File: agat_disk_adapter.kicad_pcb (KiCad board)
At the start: 2 copper layers, 58.4 x 50.8 mm, 9 parts, among them J1 Controller, J2_A1 IZOT FDD, J2_B2 IZOT FDD, J3 Apple II FDD, J4 Gotek, J5 Gotek power, J6 DS switch, J7 Jumper parking, J8 Controller DS2

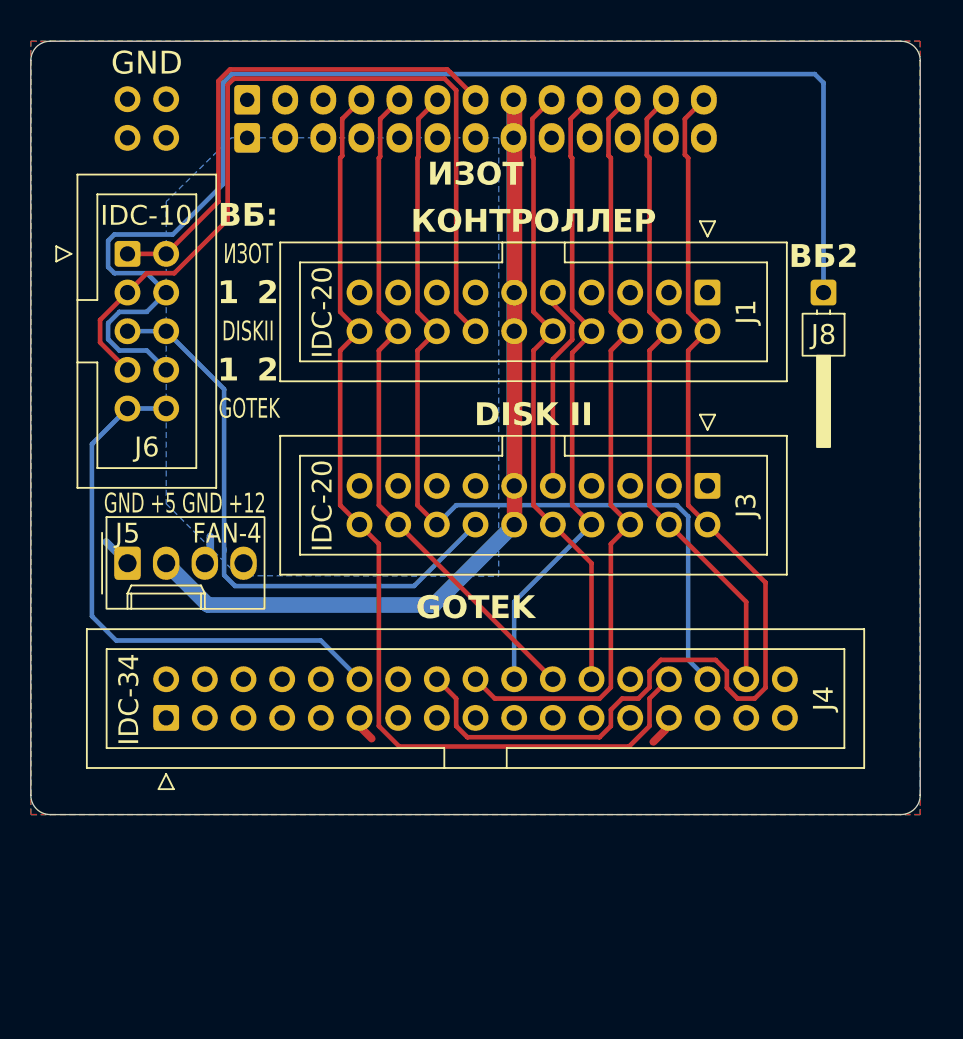
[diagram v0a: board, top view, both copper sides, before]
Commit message: one fdc connector
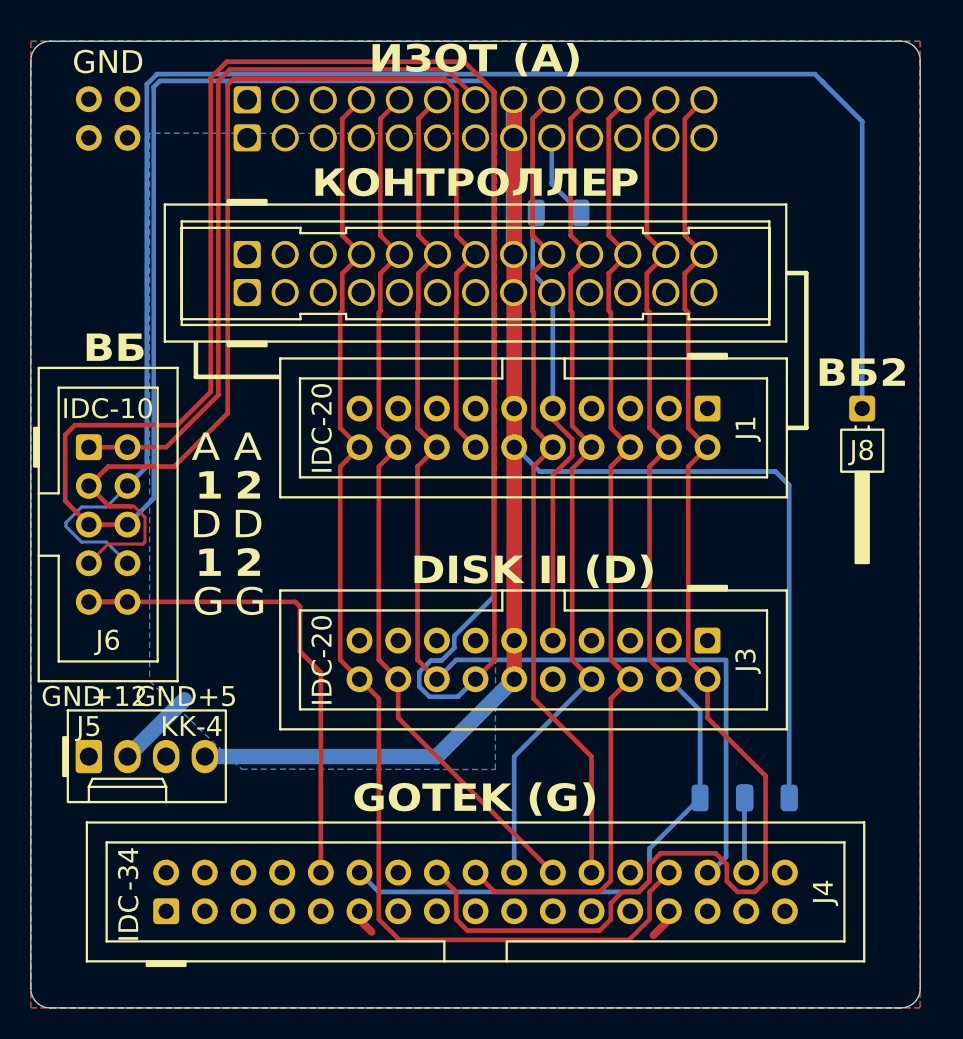
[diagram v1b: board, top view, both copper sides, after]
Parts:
- added J9_A1: КОНТРОЛЛЕР, Connector_JST:JST_EH_B13B-EH-A_1x13_P2.50mm_Vertical, F.Cu at (68.6, 55.9)
- added J9_B2: КОНТРОЛЛЕР, Connector_JST:JST_EH_B13B-EH-A_1x13_P2.50mm_Vertical, F.Cu at (68.6, 53.4)
- added R1: 0, Resistor_SMD:R_1206_3216Metric, B.Cu at (74.0, 50.6)
- added R2: 0, Resistor_SMD:R_1206_3216Metric, B.Cu at (87.7, 89.1)
- added R3: 0, Resistor_SMD:R_1206_3216Metric, B.Cu at (84.8, 89.1)
- J1: value Controller -> КОНТРОЛЛЕР
- J2_A1, J2_B2: value IZOT FDD -> ИЗОТ
- J3: value Apple II FDD -> DISK II
- J4: value Gotek -> GOTEK
- J5: value Gotek power -> Питание GOTEK
- J6: value DS switch -> ВБ
- J7: value Jumper parking -> Джамперы
- J8: value Controller DS2 -> ВБ2
- moved J5 13.0 mm to (43.2, 86.4)
- moved J6 13.0 mm to (43.2, 66.0)
- moved J4 12.7 mm to (48.3, 96.5)
- moved J3 10.2 mm to (83.8, 78.7)
- moved J8 8.03 mm to (94.0, 63.5)
- moved J1 7.62 mm to (83.8, 63.5)
- moved J7 2.54 mm to (43.2, 43.2)
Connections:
- net /DS1 renamed /EN1
- net /DS_J2 renamed /EN_J2
- net /DS_J3 renamed /EN_J3
- net /F0 renamed /PH0
- net /F2 renamed /PH2
- net /F3 renamed /PH3
- J1 pad 4: /F1 -> /PH1
- J2_A1 pad 9: unconnected-(J2_A1-Pin_9-Pad9) -> Net-(J2_A1-Pin_9)
- J2_B2 pad 12: /F1 -> /PH1
- J3 pad 4: /F1 -> /PH1
- J4 pad 10: unconnected-(J4-Pin_10-Pad10) -> /EN_J4
- J4 pad 12: /DS_J4 -> /PH1
- J4 pad 32: /F1 -> Net-(J4-Pin_32)
- J5 pad 2: /+5 -> /+12
- J5 pad 4: /+12 -> /+5
- J6 pad 10: /DS_J4 -> /EN_J4
- J6 pad 4: /DS2 -> /EN2
- J6 pad 8: /DS2 -> /EN2
- J6 pad 9: /DS_J4 -> /EN_J4
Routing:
- net /EN_J3: track 38.9 -> 200.2 mm
- net /PH1: track 0.00 -> 76.6 mm
- net /+5: track 80.8 -> 147.4 mm
- net /F1: track 42.3 -> 0.00 mm
- net /DS_J4: track 36.4 -> 0.00 mm
- net /EN_J4: track 0.00 -> 34.6 mm
- net /EN1: track 55.8 -> 83.6 mm
- net /DS2: track 86.0 -> 106.3 mm
- net /RD: track 58.6 -> 75.1 mm
- net /-12: track 13.9 -> 29.1 mm
- net /EN_J2: track 33.5 -> 48.6 mm
- net /WRP: track 67.1 -> 80.8 mm
- net /WR: track 44.4 -> 58.1 mm
- net /PH0: track 72.7 -> 86.4 mm
- net /PH2: track 51.0 -> 64.7 mm
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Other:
- board size 58.4 x 50.8 mm -> 58.4 x 63.5 mm
- board text added: "0"
- board text added: "A"
- board text added: "D"
- board text added: "DISK II (D)"
- board text added: "G"
- board text added: "GOTEK (G)"
- board text added: "IDC"
- board text added: "J9"
- board text added: "KK‐4"
- board text added: "PH1"
- board text added: "R1"
- board text added: "ВБ"
- board text added: "ИЗОТ (A)"
- board text added: "‐34"
- board text removed: "DISK II"
- board text removed: "DISKII"
- board text removed: "FAN-4"
- board text removed: "GND +5 GND +12"
- board text removed: "GOTEK"
- board text removed: "IDC‐34"
- board text removed: "ВБ:"
- board text removed: "ИЗОТ"
- board text removed: "⊢ +12 ⊣"
- board text removed: "⊢ GND ⊣"
- board text removed: "⊢-------- GND --------⊣"
